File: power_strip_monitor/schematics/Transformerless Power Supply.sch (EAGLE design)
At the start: 7 parts, among them IC1 LM2936DT-3.0, IC2 LM2936DT-3.0

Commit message: Kevin's working on the board
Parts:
- removed IC1, IC2: LM2936DT-3.0, national-semiconductor:LM2936DT-3.0
- added U1, U2: MCP1825, Cool_Electricity:MCP1825
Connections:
- net +5V: now also U1.VOUT; no longer IC1.VO
- net GND: now also U1.GND, U1.TAB, U2.GND, U2.TAB; no longer IC1.GND, IC2.GND
- net LINE: now also U1.VIN, U2.VIN; no longer IC1.VIN, IC2.VIN
- net NEUTRAL: now also U2.VOUT; no longer IC2.VO
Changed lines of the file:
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@@
 <?xml version="1.0" encoding="utf-8"?>
 <!DOCTYPE eagle SYSTEM "eagle.dtd">
-<eagle version="6.2">
+<eagle version="6.1">
 <drawing>
 <settings>
@@
 <part name="C2" library="resistor" deviceset="C-US" device="025-024X044"/>
 <part name="GND1" library="supply1" deviceset="GND" device=""/>
-<part name="LINE" library="supply2" deviceset="VCC" device=""/>
-<part name="NEUTRAL" library="supply2" deviceset="VDD" device=""/>
-<part name="IC1" library="national-semiconductor" deviceset="LM2936?*" device="DT" technology="-3.0"/>
-<part name="IC2" library="national-semiconductor" deviceset="LM2936?*" device="DT" technology="-3.0"/>
 <part name="GND2" library="supply1" deviceset="GND" device=""/>
 <part name="GND3" library="supply1" deviceset="GND" device=""/>
 <part name="+3V1" library="supply1" deviceset="+3V3" device=""/>
 <part name="P+1" library="supply1" deviceset="+5V" device=""/>
+<part name="U1" library="Cool_Electricity" deviceset="MCP1825" device=""/>
+<part name="U2" library="Cool_Electricity" deviceset="MCP1825" device=""/>
 </parts>
 <sheets>
@@
 <instance part="C2" gate="G$1" x="99.06" y="63.5"/>
 <instance part="GND1" gate="1" x="99.06" y="40.64"/>
-<instance part="LINE" gate="G$1" x="38.1" y="78.74"/>
-<instance part="NEUTRAL" gate="G$1" x="38.1" y="53.34"/>
-<instance part="IC1" gate="G$1" x="127" y="81.28"/>
-<instance part="IC2" gate="G$1" x="127" y="50.8"/>
 <instance part="GND2" gate="1" x="127" y="66.04"/>
 <instance part="GND3" gate="1" x="127" y="35.56"/>
-<instance part="+3V1" gate="G$1" x="142.24" y="58.42"/>
-<instance part="P+1" gate="1" x="142.24" y="91.44"/>
+<instance part="+3V1" gate="G$1" x="147.32" y="58.42"/>
+<instance part="P+1" gate="1" x="152.4" y="91.44"/>
+<instance part="U1" gate="G$1" x="127" y="81.28"/>
+<instance part="U2" gate="G$1" x="127" y="50.8"/>
 </instances>
 <busses>
@@
 </segment>
 <segment>
-<pinref part="IC1" gate="G$1" pin="GND"/>
 <pinref part="GND2" gate="1" pin="GND"/>
-<wire x1="127" y1="73.66" x2="127" y2="68.58" width="0.1524" layer="91"/>
+<wire x1="127" y1="73.66" x2="127" y2="71.12" width="0.1524" layer="91"/>
+<pinref part="U1" gate="G$1" pin="GND"/>
+<pinref part="U1" gate="G$1" pin="TAB"/>
+<wire x1="127" y1="71.12" x2="127" y2="68.58" width="0.1524" layer="91"/>
+<wire x1="129.54" y1="73.66" x2="129.54" y2="71.12" width="0.1524" layer="91"/>
+<wire x1="129.54" y1="71.12" x2="127" y2="71.12" width="0.1524" layer="91"/>
+<junction x="127" y="71.12"/>
 </segment>
 <segment>
-<pinref part="IC2" gate="G$1" pin="GND"/>
 <pinref part="GND3" gate="1" pin="GND"/>
-<wire x1="127" y1="43.18" x2="127" y2="38.1" width="0.1524" layer="91"/>
+<wire x1="127" y1="43.18" x2="127" y2="40.64" width="0.1524" layer="91"/>
+<pinref part="U2" gate="G$1" pin="GND"/>
+<pinref part="U2" gate="G$1" pin="TAB"/>
+<wire x1="127" y1="40.64" x2="127" y2="38.1" width="0.1524" layer="91"/>
+<wire x1="129.54" y1="43.18" x2="129.54" y2="40.64" width="0.1524" layer="91"/>
+<wire x1="129.54" y1="40.64" x2="127" y2="40.64" width="0.1524" layer="91"/>
+<junction x="127" y="40.64"/>
 </segment>
 </net>
@@
 <pinref part="C2" gate="G$1" pin="1"/>
 <wire x1="99.06" y1="73.66" x2="99.06" y2="66.04" width="0.1524" layer="91"/>
-<wire x1="73.66" y1="73.66" x2="38.1" y2="73.66" width="0.1524" layer="91"/>
-<pinref part="LINE" gate="G$1" pin="VCC"/>
-<wire x1="38.1" y1="73.66" x2="38.1" y2="76.2" width="0.1524" layer="91"/>
-<pinref part="IC1" gate="G$1" pin="VIN"/>
+<wire x1="73.66" y1="73.66" x2="25.4" y2="73.66" width="0.1524" layer="91"/>
 <wire x1="99.06" y1="73.66" x2="99.06" y2="83.82" width="0.1524" layer="91"/>
 <wire x1="99.06" y1="83.82" x2="111.76" y2="83.82" width="0.1524" layer="91"/>
-<pinref part="IC2" gate="G$1" pin="VIN"/>
 <wire x1="111.76" y1="83.82" x2="116.84" y2="83.82" width="0.1524" layer="91"/>
 <wire x1="111.76" y1="83.82" x2="111.76" y2="53.34" width="0.1524" layer="91"/>
 <wire x1="111.76" y1="53.34" x2="116.84" y2="53.34" width="0.1524" layer="91"/>
+<pinref part="U1" gate="G$1" pin="VIN"/>
+<pinref part="U2" gate="G$1" pin="VIN"/>
+<label x="25.4" y="73.66" size="1.778" layer="95"/>
 </segment>
 </net>
@@
 <pinref part="R1" gate="G$1" pin="1"/>
 <wire x1="40.64" y1="48.26" x2="38.1" y2="48.26" width="0.1524" layer="91"/>
-<pinref part="NEUTRAL" gate="G$1" pin="VDD"/>
-<wire x1="38.1" y1="48.26" x2="38.1" y2="50.8" width="0.1524" layer="91"/>
-<pinref part="IC2" gate="G$1" pin="VO"/>
-<wire x1="137.16" y1="53.34" x2="142.24" y2="53.34" width="0.1524" layer="91"/>
-<wire x1="142.24" y1="53.34" x2="142.24" y2="27.94" width="0.1524" layer="91"/>
-<wire x1="142.24" y1="27.94" x2="38.1" y2="27.94" width="0.1524" layer="91"/>
+<wire x1="142.24" y1="53.34" x2="147.32" y2="53.34" width="0.1524" layer="91"/>
+<wire x1="147.32" y1="53.34" x2="147.32" y2="27.94" width="0.1524" layer="91"/>
+<wire x1="147.32" y1="27.94" x2="38.1" y2="27.94" width="0.1524" layer="91"/>
 <wire x1="38.1" y1="27.94" x2="38.1" y2="48.26" width="0.1524" layer="91"/>
 <pinref part="+3V1" gate="G$1" pin="+3V3"/>
-<wire x1="142.24" y1="53.34" x2="142.24" y2="55.88" width="0.1524" layer="91"/>
+<wire x1="147.32" y1="53.34" x2="147.32" y2="55.88" width="0.1524" layer="91"/>
+<pinref part="U2" gate="G$1" pin="VOUT"/>
+<label x="25.4" y="48.26" size="1.778" layer="95"/>
+<wire x1="38.1" y1="48.26" x2="25.4" y2="48.26" width="0.1524" layer="91"/>
+<junction x="38.1" y="48.26"/>
 </segment>
 </net>
 <net name="+5V" class="0">
 <segment>
-<pinref part="IC1" gate="G$1" pin="VO"/>
-<wire x1="137.16" y1="83.82" x2="142.24" y2="83.82" width="0.1524" layer="91"/>
+<wire x1="149.86" y1="83.82" x2="152.4" y2="86.36" width="0.1524" layer="91"/>
 <pinref part="P+1" gate="1" pin="+5V"/>
-<wire x1="142.24" y1="83.82" x2="142.24" y2="88.9" width="0.1524" layer="91"/>
+<wire x1="152.4" y1="86.36" x2="152.4" y2="88.9" width="0.1524" layer="91"/>
+<pinref part="U1" gate="G$1" pin="VOUT"/>
+<wire x1="149.86" y1="83.82" x2="142.24" y2="83.82" width="0.1524" layer="91"/>
 </segment>
 </net>

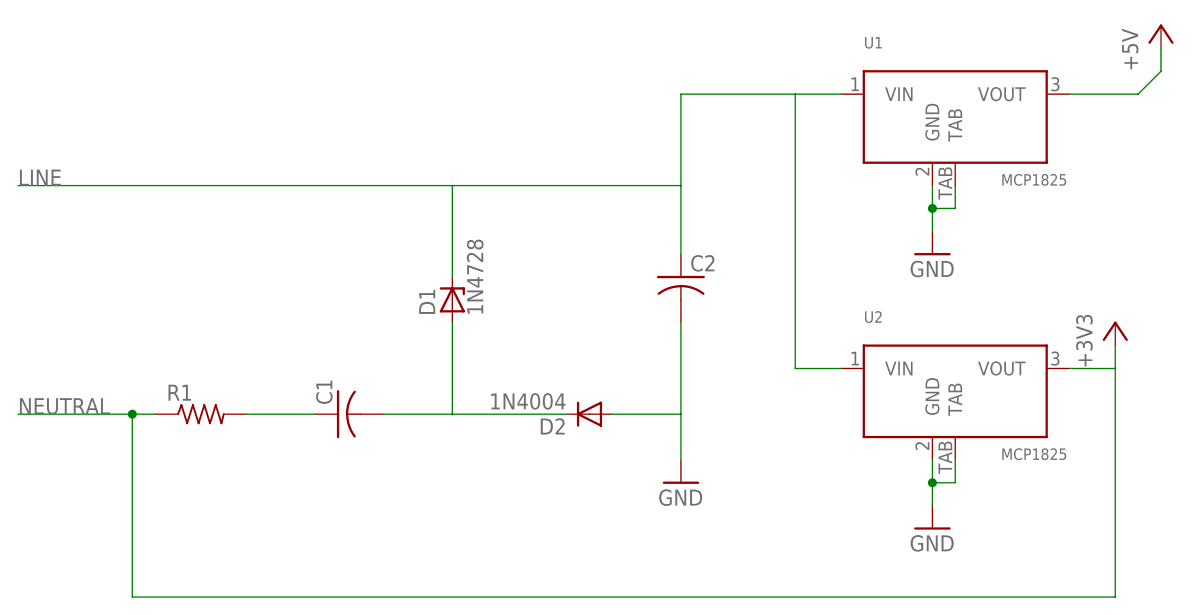
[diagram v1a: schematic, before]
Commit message: Added LEDs on schematic and layout
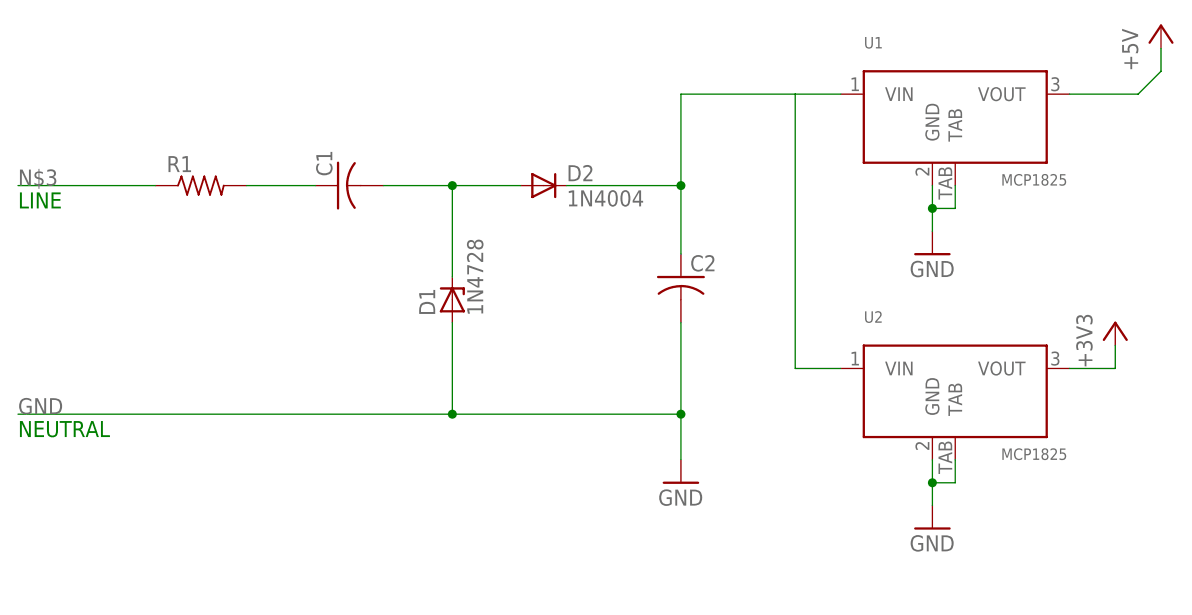
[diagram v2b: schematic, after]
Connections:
- removed net N$2: C1.2, D1.A, D2.C
- new net N$3: C1.2, D1.C, D2.A
- net GND: now also D1.A; no longer D2.A
- net LINE: now also D2.C, R1.1; no longer D1.C
- net NEUTRAL: no longer R1.1
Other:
- note added: "LINE"
- note added: "NEUTRAL"
- moved on the sheet: C1, D2, R1
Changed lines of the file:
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@@
 <?xml version="1.0" encoding="utf-8"?>
 <!DOCTYPE eagle SYSTEM "eagle.dtd">
-<eagle version="6.1">
+<eagle version="6.2">
 <drawing>
 <settings>
@@
 <sheet>
 <plain>
+<text x="25.4" y="71.12" size="1.778" layer="91">LINE</text>
+<text x="25.4" y="45.72" size="1.778" layer="91">NEUTRAL</text>
 </plain>
 <instances>
 <instance part="D1" gate="1" x="73.66" y="60.96" rot="R90"/>
-<instance part="D2" gate="1" x="88.9" y="48.26" rot="R180"/>
-<instance part="C1" gate="G$1" x="60.96" y="48.26" rot="R90"/>
-<instance part="R1" gate="G$1" x="45.72" y="48.26"/>
+<instance part="D2" gate="1" x="83.82" y="73.66"/>
+<instance part="C1" gate="G$1" x="60.96" y="73.66" rot="R90"/>
+<instance part="R1" gate="G$1" x="45.72" y="73.66"/>
 <instance part="C2" gate="G$1" x="99.06" y="63.5"/>
 <instance part="GND1" gate="1" x="99.06" y="40.64"/>
@@
 </busses>
 <nets>
-<net name="N$1" class="0">
-<segment>
-<pinref part="R1" gate="G$1" pin="2"/>
-<pinref part="C1" gate="G$1" pin="1"/>
-<wire x1="50.8" y1="48.26" x2="58.42" y2="48.26" width="0.1524" layer="91"/>
-</segment>
-</net>
-<net name="N$2" class="0">
-<segment>
-<pinref part="C1" gate="G$1" pin="2"/>
-<pinref part="D2" gate="1" pin="C"/>
-<wire x1="66.04" y1="48.26" x2="73.66" y2="48.26" width="0.1524" layer="91"/>
-<pinref part="D1" gate="1" pin="A"/>
-<wire x1="73.66" y1="48.26" x2="86.36" y2="48.26" width="0.1524" layer="91"/>
-<wire x1="73.66" y1="58.42" x2="73.66" y2="48.26" width="0.1524" layer="91"/>
-</segment>
-</net>
 <net name="GND" class="0">
 <segment>
 <pinref part="C2" gate="G$1" pin="2"/>
 <wire x1="99.06" y1="58.42" x2="99.06" y2="48.26" width="0.1524" layer="91"/>
-<pinref part="D2" gate="1" pin="A"/>
-<wire x1="99.06" y1="48.26" x2="91.44" y2="48.26" width="0.1524" layer="91"/>
 <pinref part="GND1" gate="1" pin="GND"/>
+<label x="25.4" y="48.26" size="1.778" layer="95"/>
+<pinref part="D1" gate="1" pin="A"/>
 <wire x1="99.06" y1="48.26" x2="99.06" y2="43.18" width="0.1524" layer="91"/>
+<wire x1="73.66" y1="58.42" x2="73.66" y2="48.26" width="0.1524" layer="91"/>
+<wire x1="25.4" y1="48.26" x2="73.66" y2="48.26" width="0.1524" layer="91"/>
+<wire x1="73.66" y1="48.26" x2="99.06" y2="48.26" width="0.1524" layer="91"/>
+<junction x="73.66" y="48.26"/>
+<junction x="99.06" y="48.26"/>
 </segment>
 <segment>
@@
 <net name="LINE" class="0">
 <segment>
-<pinref part="D1" gate="1" pin="C"/>
-<wire x1="73.66" y1="63.5" x2="73.66" y2="73.66" width="0.1524" layer="91"/>
-<wire x1="73.66" y1="73.66" x2="99.06" y2="73.66" width="0.1524" layer="91"/>
 <pinref part="C2" gate="G$1" pin="1"/>
-<wire x1="99.06" y1="73.66" x2="99.06" y2="66.04" width="0.1524" layer="91"/>
-<wire x1="73.66" y1="73.66" x2="25.4" y2="73.66" width="0.1524" layer="91"/>
+<wire x1="99.06" y1="66.04" x2="99.06" y2="73.66" width="0.1524" layer="91"/>
 <wire x1="99.06" y1="73.66" x2="99.06" y2="83.82" width="0.1524" layer="91"/>
 <wire x1="99.06" y1="83.82" x2="111.76" y2="83.82" width="0.1524" layer="91"/>
@@
 <pinref part="U1" gate="G$1" pin="VIN"/>
 <pinref part="U2" gate="G$1" pin="VIN"/>
-<label x="25.4" y="73.66" size="1.778" layer="95"/>
+<pinref part="D2" gate="1" pin="C"/>
+<wire x1="86.36" y1="73.66" x2="99.06" y2="73.66" width="0.1524" layer="91"/>
+<junction x="99.06" y="73.66"/>
+</segment>
+<segment>
+<pinref part="R1" gate="G$1" pin="1"/>
+<wire x1="25.4" y1="73.66" x2="40.64" y2="73.66" width="0.1524" layer="91"/>
 </segment>
 </net>
 <net name="NEUTRAL" class="0">
 <segment>
-<pinref part="R1" gate="G$1" pin="1"/>
-<wire x1="40.64" y1="48.26" x2="38.1" y2="48.26" width="0.1524" layer="91"/>
 <wire x1="142.24" y1="53.34" x2="147.32" y2="53.34" width="0.1524" layer="91"/>
-<wire x1="147.32" y1="53.34" x2="147.32" y2="27.94" width="0.1524" layer="91"/>
-<wire x1="147.32" y1="27.94" x2="38.1" y2="27.94" width="0.1524" layer="91"/>
-<wire x1="38.1" y1="27.94" x2="38.1" y2="48.26" width="0.1524" layer="91"/>
 <pinref part="+3V1" gate="G$1" pin="+3V3"/>
 <wire x1="147.32" y1="53.34" x2="147.32" y2="55.88" width="0.1524" layer="91"/>
 <pinref part="U2" gate="G$1" pin="VOUT"/>
-<label x="25.4" y="48.26" size="1.778" layer="95"/>
-<wire x1="38.1" y1="48.26" x2="25.4" y2="48.26" width="0.1524" layer="91"/>
-<junction x="38.1" y="48.26"/>
 </segment>
 </net>
@@
 </segment>
 </net>
+<net name="N$3" class="0">
+<segment>
+<pinref part="D1" gate="1" pin="C"/>
+<wire x1="73.66" y1="63.5" x2="73.66" y2="73.66" width="0.1524" layer="91"/>
+<label x="25.4" y="73.66" size="1.778" layer="95"/>
+<pinref part="C1" gate="G$1" pin="2"/>
+<wire x1="66.04" y1="73.66" x2="73.66" y2="73.66" width="0.1524" layer="91"/>
+<pinref part="D2" gate="1" pin="A"/>
+<wire x1="73.66" y1="73.66" x2="81.28" y2="73.66" width="0.1524" layer="91"/>
+<junction x="73.66" y="73.66"/>
+</segment>
+</net>
+<net name="N$5" class="0">
+<segment>
+<pinref part="R1" gate="G$1" pin="2"/>
+<pinref part="C1" gate="G$1" pin="1"/>
+<wire x1="50.8" y1="73.66" x2="58.42" y2="73.66" width="0.1524" layer="91"/>
+</segment>
+</net>
